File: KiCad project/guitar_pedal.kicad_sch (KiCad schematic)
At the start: 49 parts, among them J1 NMJ6HCD2, J2 NMJ6HCD2, J3 AVR-ISP-6, SW1 SW_SPST, SW2 SWITCH_3PDT, U1 ATmega1284-P, U2 L7805, U3 TL061, U4 TL061, Y1 Crystal 16MHz

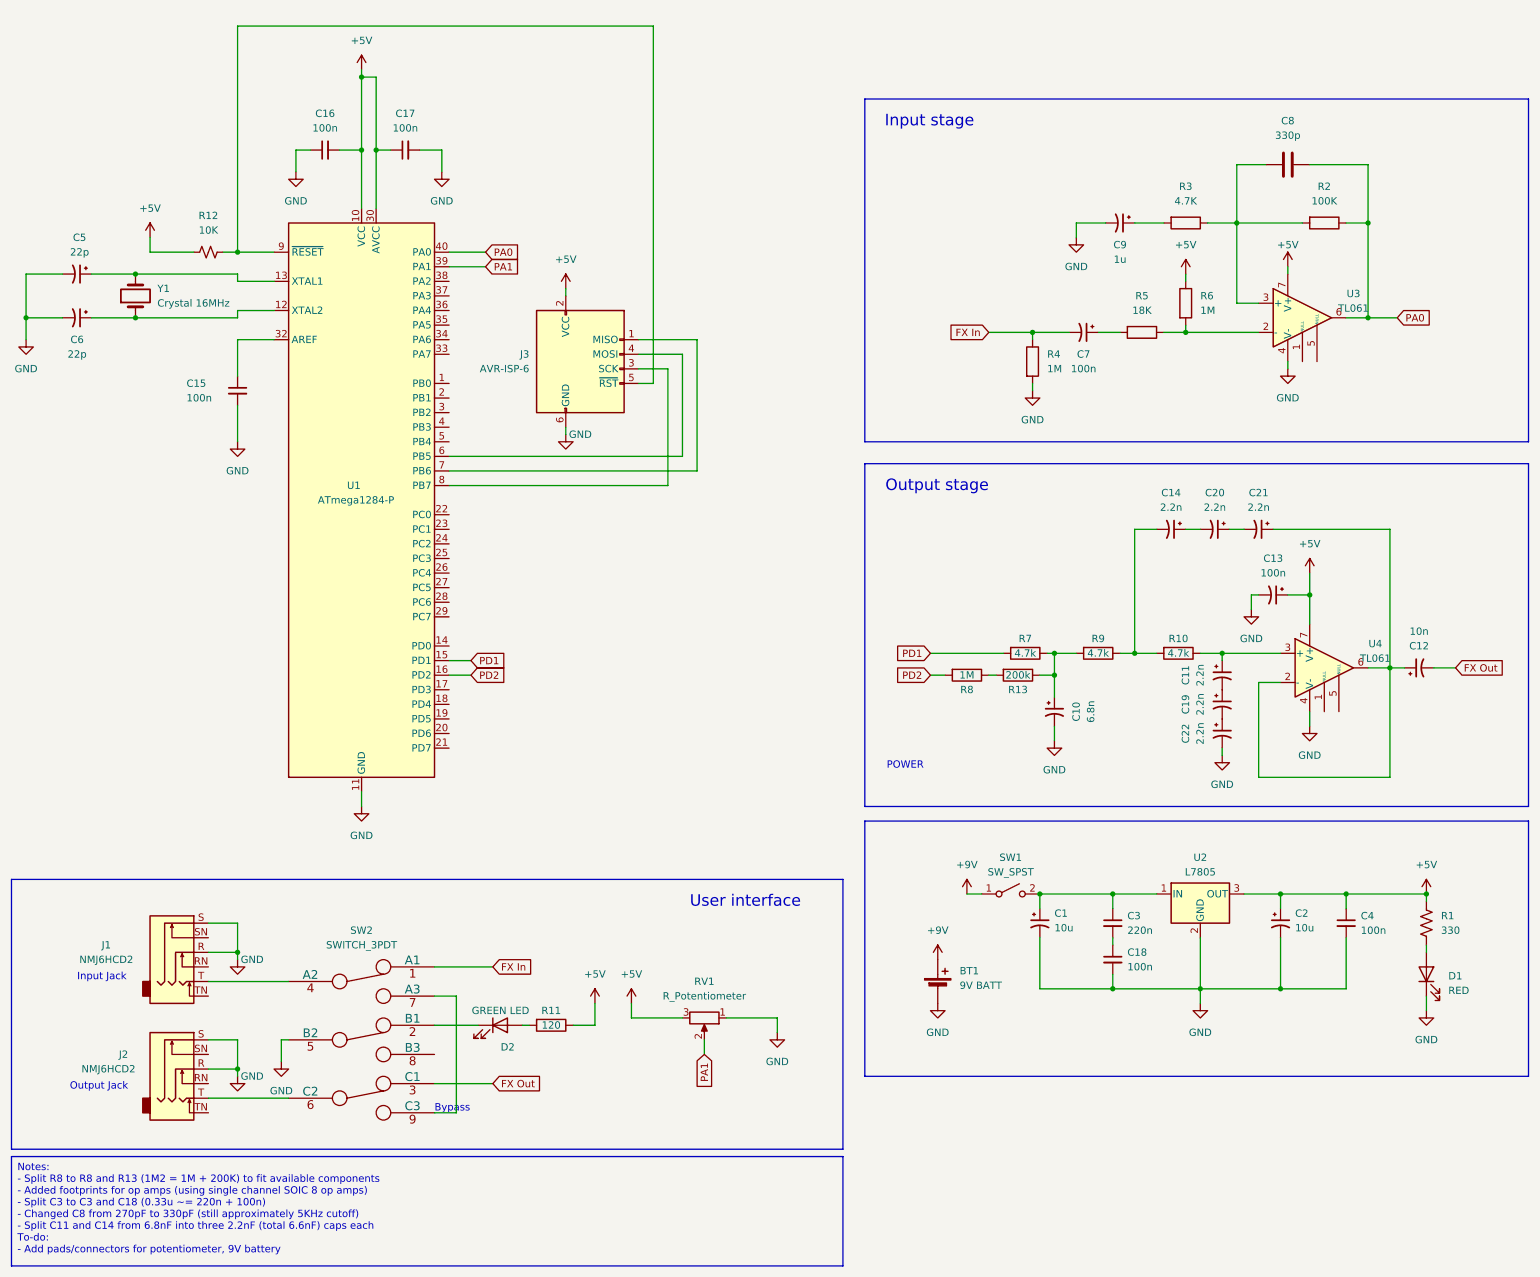
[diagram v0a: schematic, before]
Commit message: Added remaining footprints to PCB, added ground plane and board edges.
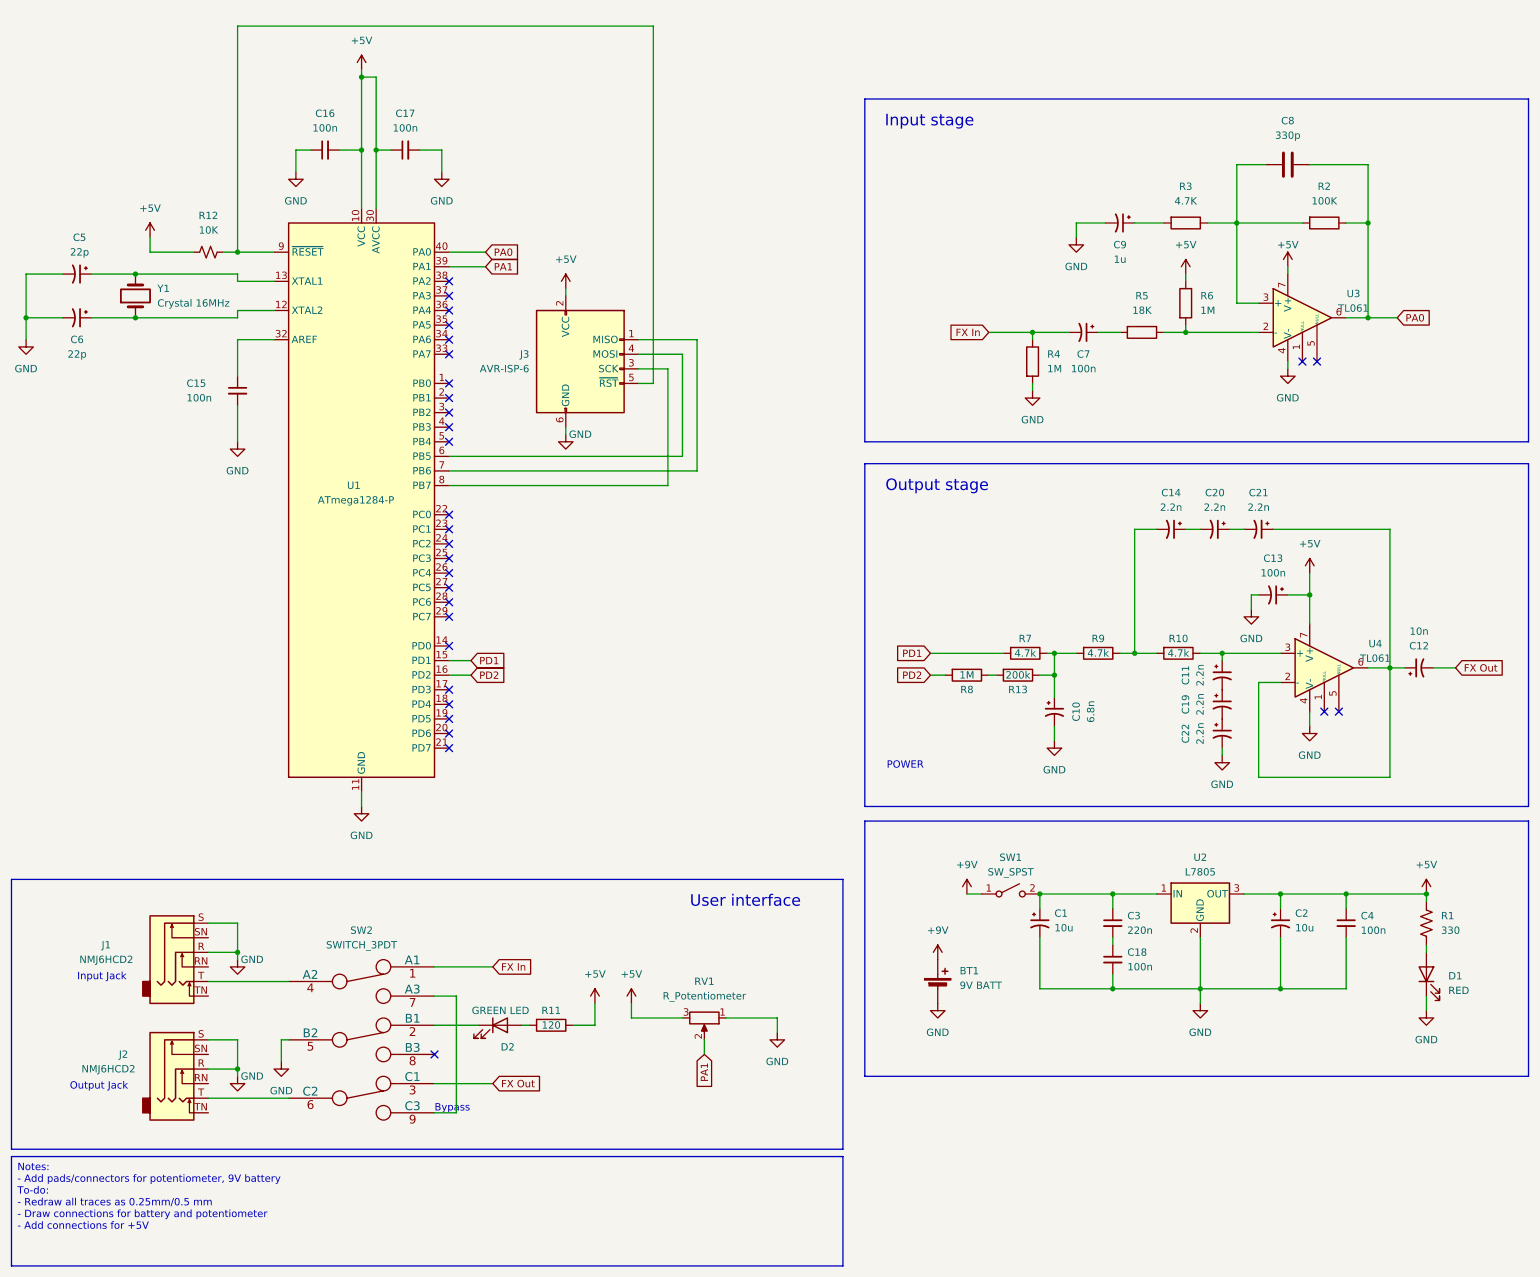
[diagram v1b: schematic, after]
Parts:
- BT1, SW1: footprint (none) -> Connector_PinHeader_2.54mm:PinHeader_1x02_P2.54mm_Vertical
- RV1: footprint (none) -> Connector_PinHeader_2.54mm:PinHeader_1x03_P2.54mm_Vertical
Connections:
- no-connect marks 0 -> 30
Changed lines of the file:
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@@
   (junction (at 212.09 185.42) (diameter 0) (color 0 0 0 0)
   )
+  (no_connect (at 96.52 85.09))
+  (no_connect (at 96.52 67.31))
+  (no_connect (at 96.52 87.63))
+  (no_connect (at 96.52 62.23))
+  (no_connect (at 96.52 74.93))
+  (no_connect (at 96.52 102.87))
+  (no_connect (at 96.52 140.97))
+  (no_connect (at 96.52 120.65))
+  (no_connect (at 96.52 69.85))
+  (no_connect (at 96.52 115.57))
+  (no_connect (at 96.52 80.01))
+  (no_connect (at 96.52 105.41))
+  (no_connect (at 96.52 118.11))
+  (no_connect (at 96.52 72.39))
+  (no_connect (at 96.52 90.17))
+  (no_connect (at 96.52 135.89))
+  (no_connect (at 96.52 143.51))
+  (no_connect (at 96.52 82.55))
+  (no_connect (at 245.11 76.2))
+  (no_connect (at 96.52 133.35))
+  (no_connect (at 96.52 64.77))
+  (no_connect (at 96.52 113.03))
+  (no_connect (at 251.46 137.16))
+  (no_connect (at 96.52 107.95))
+  (no_connect (at 93.98 196.85))
+  (no_connect (at 248.92 137.16))
+  (no_connect (at 247.65 76.2))
+  (no_connect (at 96.52 125.73))
+  (no_connect (at 96.52 138.43))
+  (no_connect (at 96.52 110.49))
   (wire (pts (xy 93.98 201.93) (xy 104.14 201.93))
     (stroke (width 0) (type default))
@@
     (fill (type none))
   )
-  (text_box "Notes:\n- Split R8 to R8 and R13 (1M2 = 1M + 200K) to fit available components\n- Added footprints for op amps (using single channel SOIC 8 op amps)\n- Split C3 to C3 and C18 (0.33u ~= 220n + 100n)\n- Changed C8 from 270pF to 330pF (still approximately 5KHz cutoff)\n- Split C11 and C14 from 6.8nF into three 2.2nF (total 6.6nF) caps each\nTo-do:\n- Add pads/connectors for potentiometer, 9V battery"
+  (text_box "Notes:\n- Add pads/connectors for potentiometer, 9V battery\nTo-do:\n- Redraw all traces as 0.25mm/0.5 mm\n- Draw connections for battery and potentiometer\n- Add connections for +5V"
     (at 20.32 214.63 0) (size 144.78 19.05)
     (stroke (width 0) (type default))
@@
       (effects (font (size 1.27 1.27)))
     )
-    (property "Footprint" "" (at 194.31 168.91 0)
+    (property "Footprint" "Connector_PinHeader_2.54mm:PinHeader_1x02_P2.54mm_Vertical" (at 194.31 168.91 0)
       (effects (font (size 1.27 1.27)) hide)
     )
@@
       (effects (font (size 1.27 1.27)) (justify left))
     )
-    (property "Footprint" "" (at 181.61 183.896 90)
+    (property "Footprint" "Connector_PinHeader_2.54mm:PinHeader_1x02_P2.54mm_Vertical" (at 181.61 183.896 90)
       (effects (font (size 1.27 1.27)) hide)
     )
@@
       (effects (font (size 1.27 1.27)))
     )
-    (property "Footprint" "" (at 140.97 190.5 0)
-      (effects (font (size 1.27 1.27)) hide)
-    )
+    (property "Footprint" "Connector_PinHeader_2.54mm:PinHeader_1x03_P2.54mm_Vertical" (at 140.97 190.5 0)
+      (effects (font (size 1.27 1.27)) hide)
+    )

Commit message: Added second layer. All connections on board. No errors in DRC, 200+ warnings.
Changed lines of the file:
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@@
     (fill (type none))
   )
-  (text_box "Notes:\n- Add pads/connectors for potentiometer, 9V battery\nTo-do:\n- Redraw all traces as 0.25mm/0.5 mm\n- Draw connections for battery and potentiometer\n- Add connections for +5V"
+  (text_box "Notes:\n- Add pads/connectors for potentiometer, 9V battery\n- Redraw all traces as 0.25mm/0.5 mm\n- Add connections for +5V\n- Draw connections for battery and potentiometer\nTo-do:\n- Edit silkscreen"
     (at 20.32 214.63 0) (size 144.78 19.05)
     (stroke (width 0) (type default))

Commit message: Design review changes. Vias added, fixed capacitors in output stage.
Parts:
- D1: footprint LED_SMD:LED_0603_1608Metric -> LED_THT:LED_D3.0mm
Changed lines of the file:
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@@
       (effects (font (size 1.27 1.27)) (justify right))
     )
-    (property "Footprint" "LED_SMD:LED_0603_1608Metric" (at 266.7 182.88 0)
+    (property "Footprint" "LED_THT:LED_D3.0mm" (at 266.7 182.88 0)
       (effects (font (size 1.27 1.27)) hide)
     )

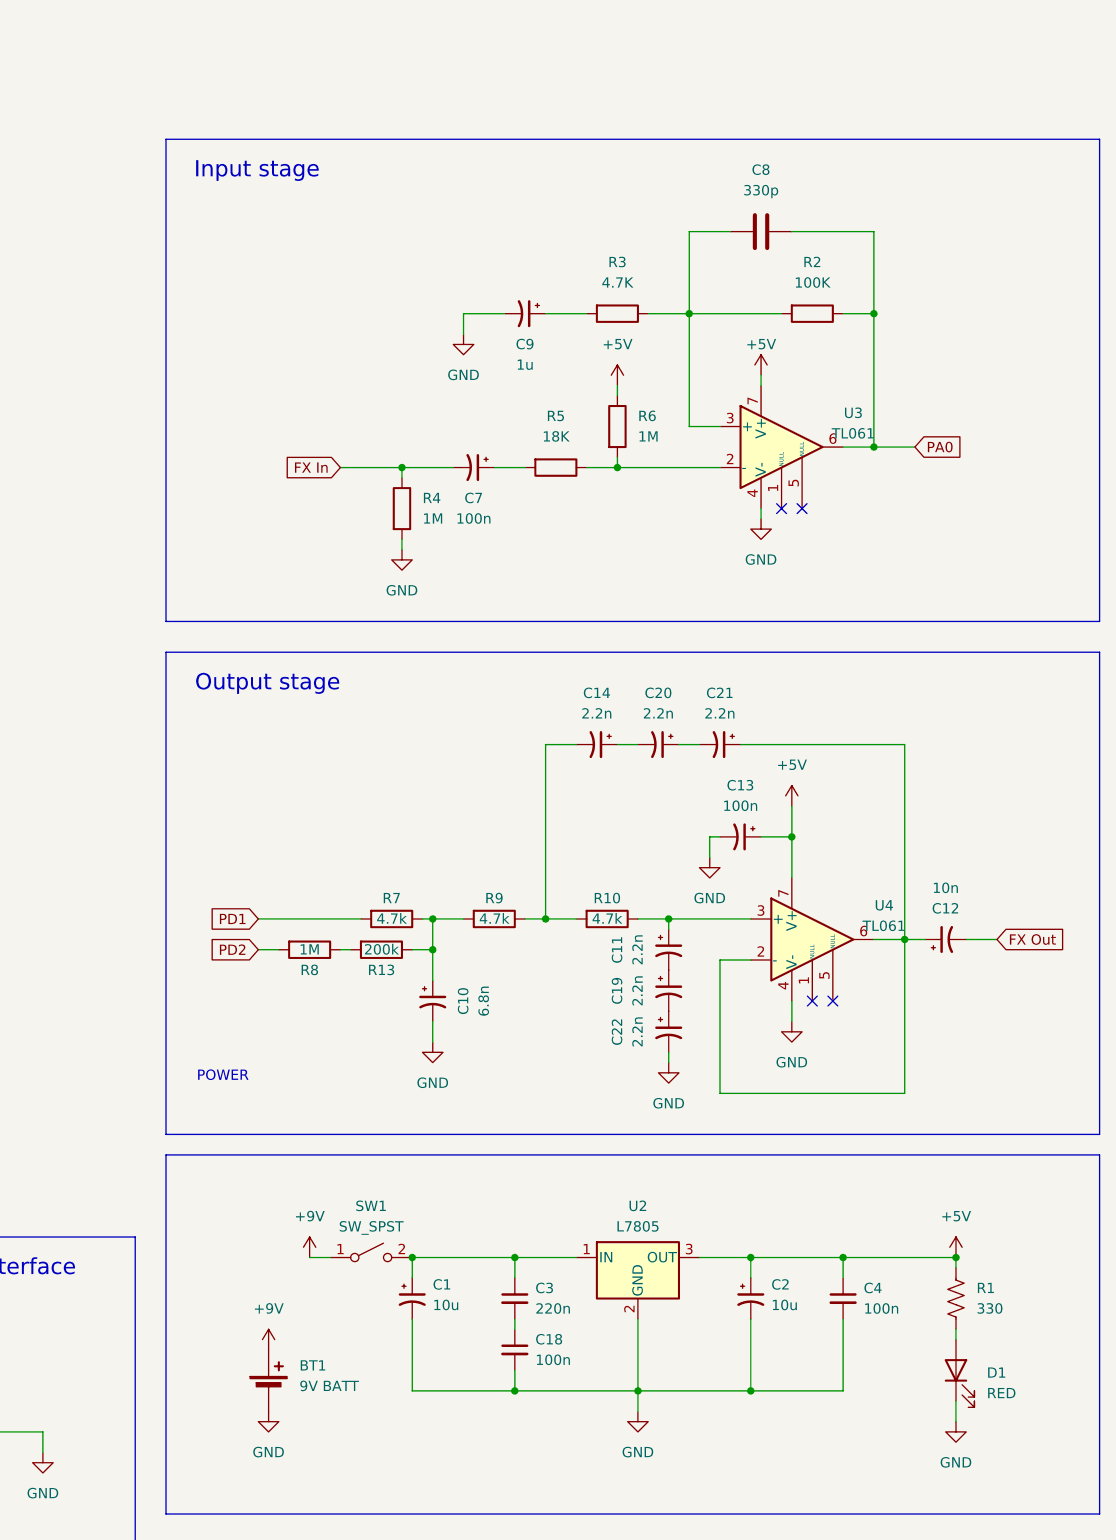
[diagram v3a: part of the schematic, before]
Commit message: Fixed cap series to parallel. Includes updated PCB and Gerber files
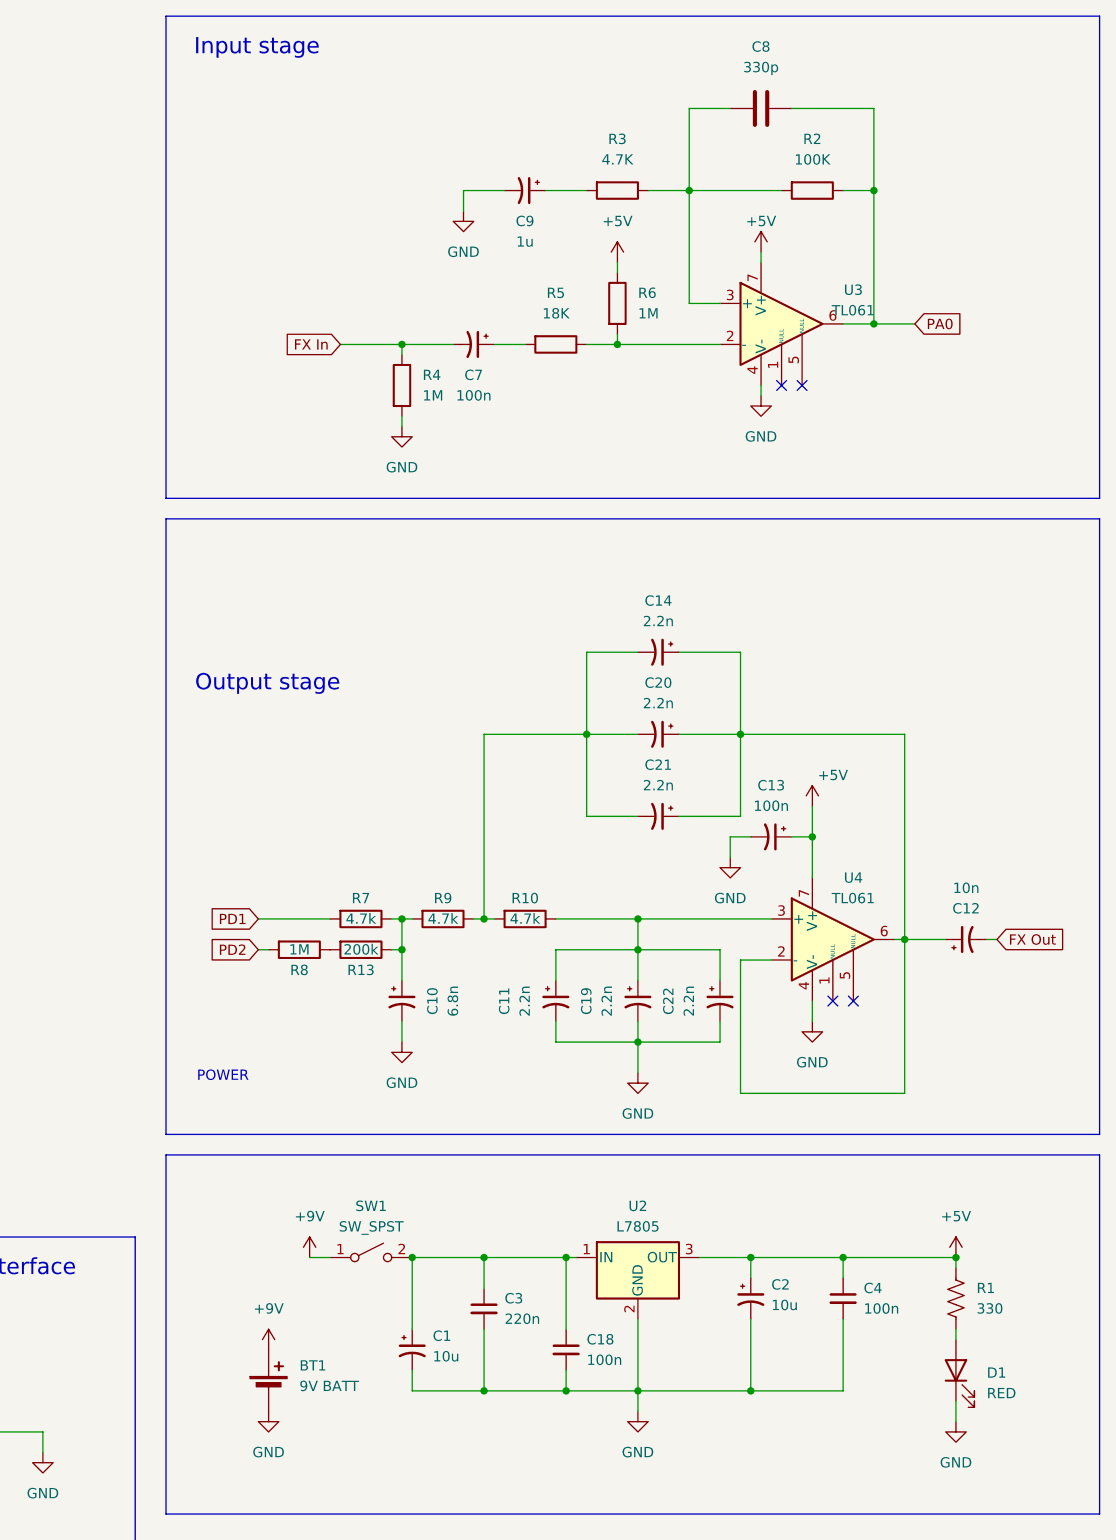
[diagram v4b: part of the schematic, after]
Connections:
- net GND: now also C11.2, C19.2, C3.2
- net at C14.2, R10.2, R9.1: now also C20.2, C21.2
- net at C1.1, C3.1, SW1.2 (B)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: now also C18.1
- net at C14.1: now also C12.1, C20.1, C21.1, U4.2 (-), U4.6; no longer C20.2
- net at C19.1: now also C11.1, C22.1, R10.1, U4.3 (+); no longer C11.2
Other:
- moved on the sheet: C1, C10, C12, C13, C18, C20, C7, C8, C9, R10, R13, R2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
